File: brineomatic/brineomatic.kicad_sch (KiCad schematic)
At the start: 11 parts, among them J1 Conn_01x04_MountingPin

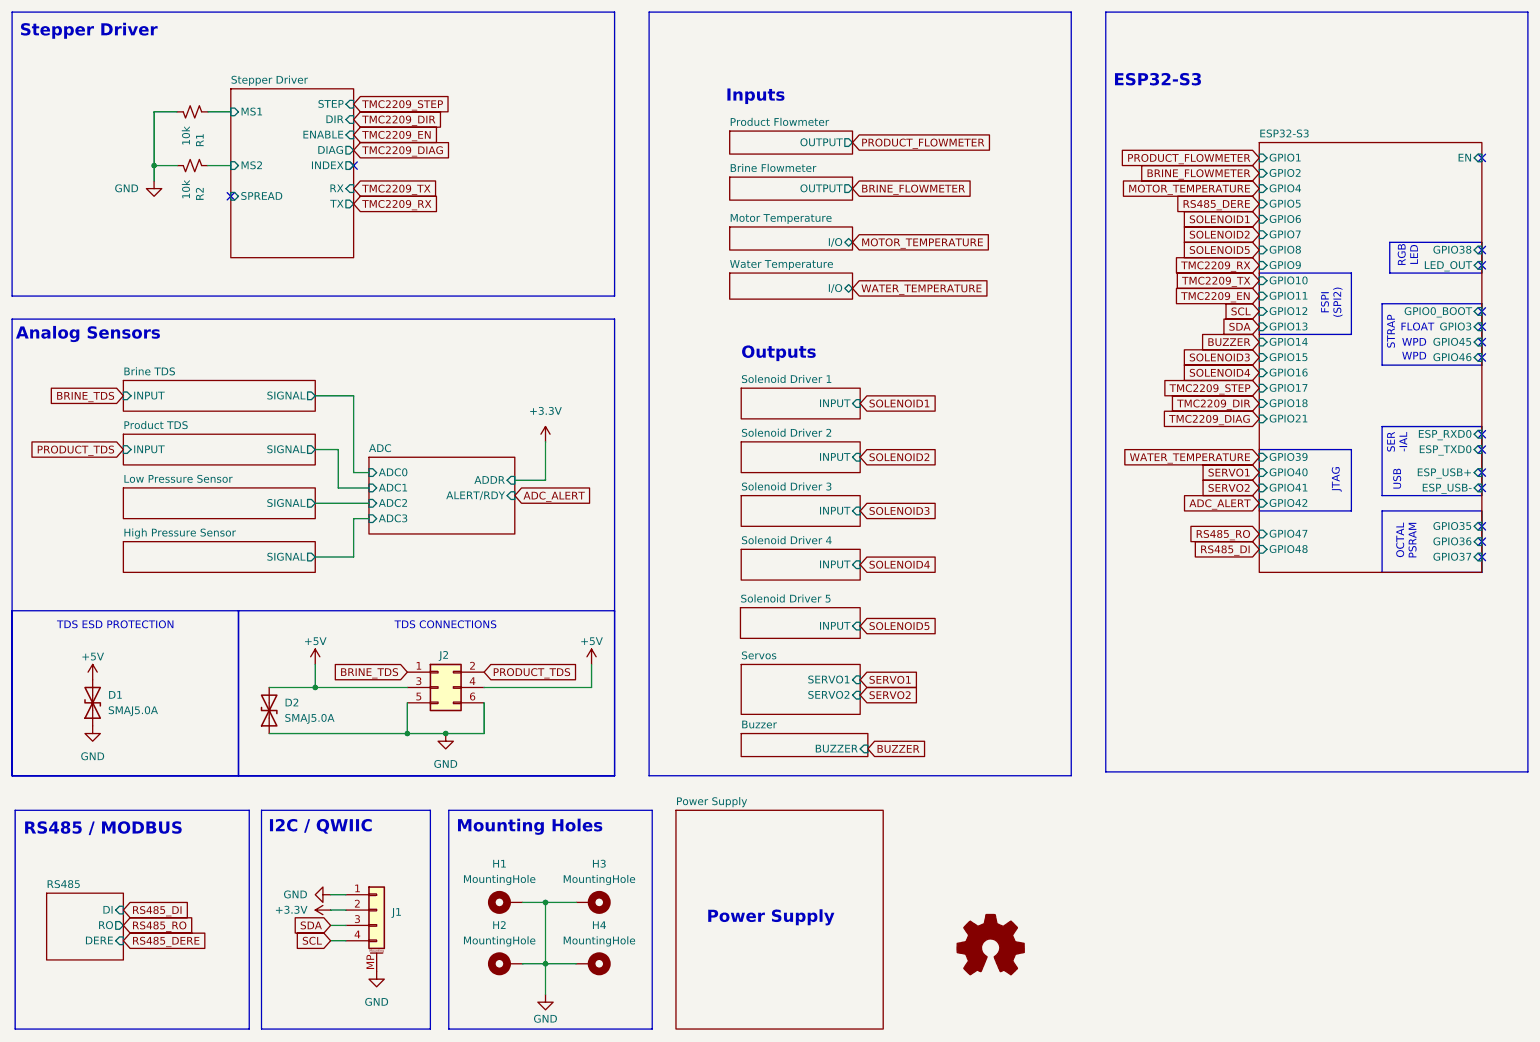
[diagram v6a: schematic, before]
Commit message: tidied up the top level schematic
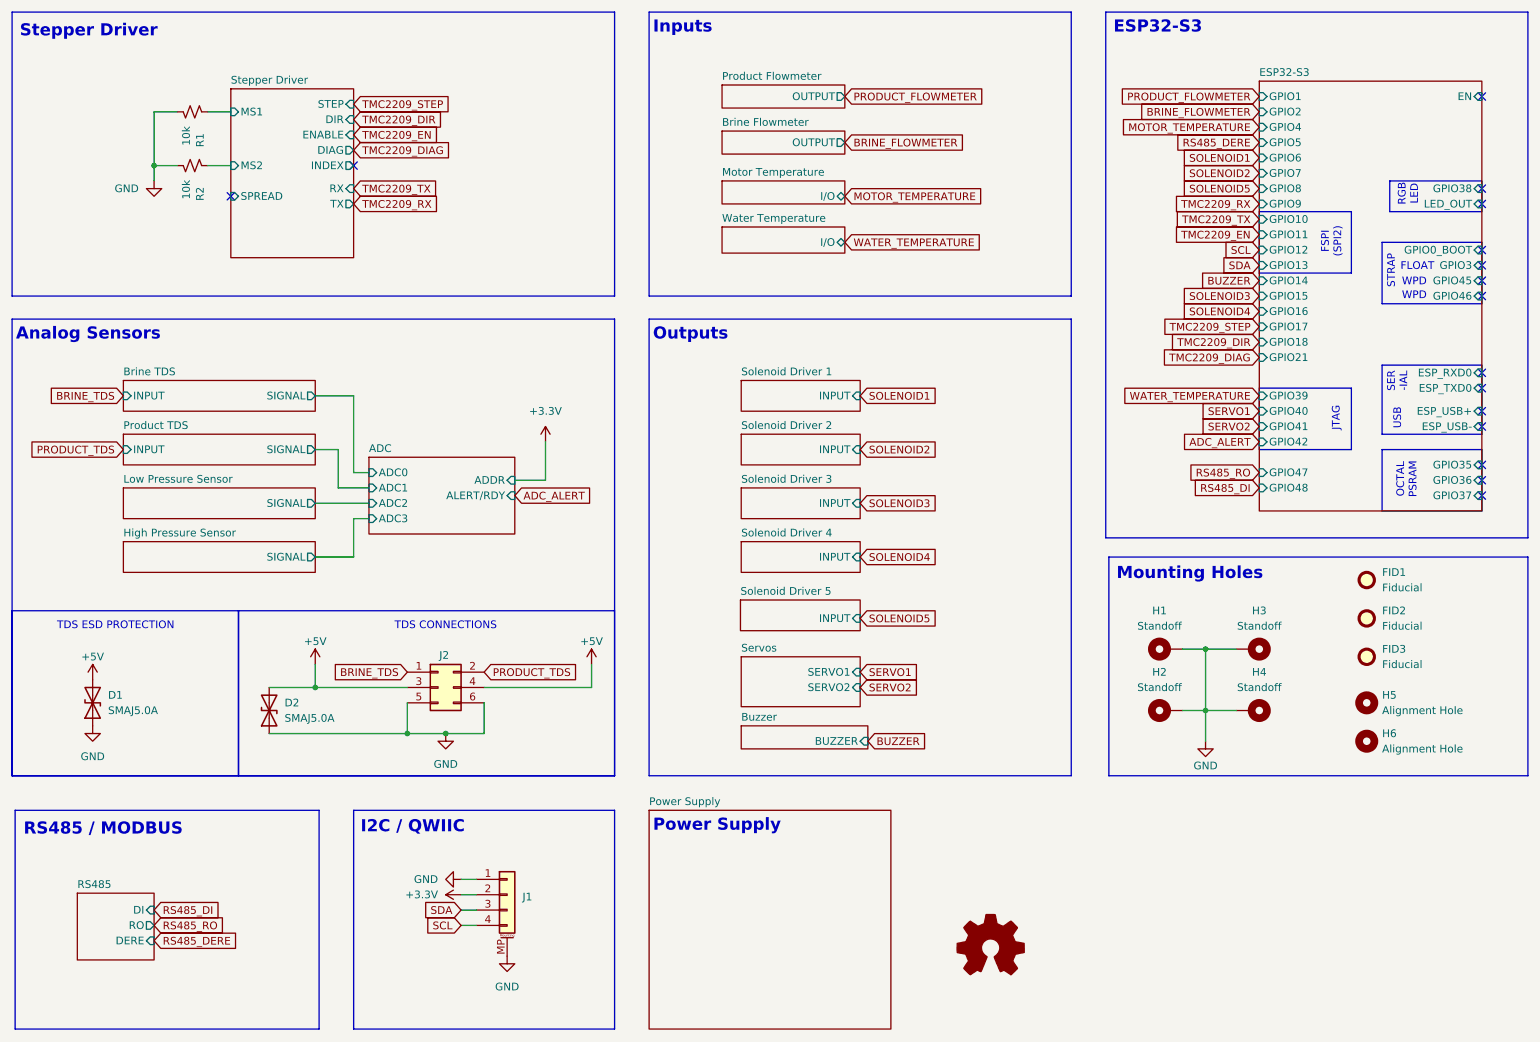
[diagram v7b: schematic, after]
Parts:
- added FID1, FID2, FID3: Fiducial, Fiducial:Fiducial_1mm_Mask2mm, symbol Mechanical:Fiducial
- added H5, H6: Alignment Hole, MountingHole:MountingHole_2.2mm_M2, symbol Mechanical:MountingHole
- H1, H2, H3, H4: value MountingHole -> Standoff
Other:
- moved on the sheet: H1, H2, H3, H4, J1

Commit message: holy re-routing batman. board is fully routed first pass.
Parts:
- renumbered J2 to J1, J1 to J2
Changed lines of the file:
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@@
 		(on_board yes)
 		(dnp no)
-		(property "Reference" "J1"
+		(property "Reference" "J2"
 			(at 107.95 165.4555 0)
 			(effects
@@
 			(project ""
 				(path "/96477ae2-ef08-48f3-8dd4-fe4478541f68"
-					(reference "J1")
+					(reference "J2")
 					(unit 1)
 				)
@@
 		(dnp no)
 		(fields_autoplaced yes)
-		(property "Reference" "#PWR06"
+		(property "Reference" "#PWR07"
 			(at 101.6 165.1 0)
 			(effects
@@
 			(project "brineomatic"
 				(path "/96477ae2-ef08-48f3-8dd4-fe4478541f68"
-					(reference "#PWR06")
+					(reference "#PWR07")
 					(unit 1)
 				)
@@
 		(on_board yes)
 		(dnp no)
-		(property "Reference" "#PWR011"
+		(property "Reference" "#PWR010"
 			(at 119.38 130.81 0)
 			(effects
@@
 			(project "brineomatic"
 				(path "/96477ae2-ef08-48f3-8dd4-fe4478541f68"
-					(reference "#PWR011")
+					(reference "#PWR010")
 					(unit 1)
 				)
@@
 		(dnp no)
 		(fields_autoplaced yes)
-		(property "Reference" "#PWR08"
+		(property "Reference" "#PWR05"
 			(at 95.25 144.78 0)
 			(effects
@@
 			(project "brineomatic"
 				(path "/96477ae2-ef08-48f3-8dd4-fe4478541f68"
-					(reference "#PWR08")
+					(reference "#PWR05")
 					(unit 1)
 				)
@@
 		(on_board yes)
 		(dnp no)
-		(property "Reference" "#PWR010"
+		(property "Reference" "#PWR011"
 			(at 220.98 146.05 0)
 			(effects
@@
 			(project "brineomatic"
 				(path "/96477ae2-ef08-48f3-8dd4-fe4478541f68"
-					(reference "#PWR010")
+					(reference "#PWR011")
 					(unit 1)
 				)
@@
 		(dnp no)
 		(fields_autoplaced yes)
-		(property "Reference" "#PWR07"
+		(property "Reference" "#PWR08"
 			(at 105.41 181.61 0)
 			(effects
@@
 			(project "brineomatic"
 				(path "/96477ae2-ef08-48f3-8dd4-fe4478541f68"
-					(reference "#PWR07")
+					(reference "#PWR08")
 					(unit 1)
 				)
@@
 		(on_board yes)
 		(dnp no)
-		(property "Reference" "J2"
+		(property "Reference" "J1"
 			(at 94.996 125.476 0)
 			(effects
@@
 			(project "brineomatic"
 				(path "/96477ae2-ef08-48f3-8dd4-fe4478541f68"
-					(reference "J2")
+					(reference "J1")
 					(unit 1)
 				)
@@
 		(dnp no)
 		(fields_autoplaced yes)
-		(property "Reference" "#PWR05"
+		(property "Reference" "#PWR06"
 			(at 91.44 162.56 0)
 			(effects
@@
 			(project "brineomatic"
 				(path "/96477ae2-ef08-48f3-8dd4-fe4478541f68"
-					(reference "#PWR05")
-					(unit 1)
-				)
+					(reference "#PWR06")
+					(unit 1)
+				)
